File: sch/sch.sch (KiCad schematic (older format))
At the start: 6 parts, among them P1 Digital, P2 Analog, P3 CONN_1, P4 CONN_1, P5 CONN_1, P6 CONN_1

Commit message: Started schematic draft
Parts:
- added D? (x18): LED, symbol LED
- added D? (x6): D_Schottky, symbol D_Schottky
- added L? (x6): INDUCTOR, symbol INDUCTOR
- added R? (x26): R, symbol R
- added U? (x6): PT4115, symbol PT4115
- added U? (x2): LM741, symbol LM741
- added U?: 74LS595, symbol 74LS595
- added U?: 74LS165, symbol 74LS165
- added U?: 7805, symbol 7805
- added U? (x2): DS18B20, symbol DS18B20
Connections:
- net labels added: +BATT, -9VA, CLK, CLK2, DIM1, DIM2, DIM3, DIM4, DIM5, DIM6, L0, L1, L2, L3, L4, L5, L6, L7, LP0, LP1, LP2, LP3, LP4, LP5, LP6, LP7, PH, SALINITY, SER_IN, SER_OUT, T0, T1, ~LD
- wire segments 35 -> 181
- no-connect marks 4 -> 6

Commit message: More schematic work
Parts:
- removed U? (x2): LM741, symbol LM741
- added C? (x2): C, symbol C
- added C? (x2): CP, symbol CP
- added P? (x2): CONN_01X02, symbol CONN_01X02
- added P?: BNC, symbol BNC
- added R?: R, symbol R
- added U? (x4): LM324, symbol LM324
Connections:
- net labels removed: -9VA
- wire segments 181 -> 193
- no-connect marks 6 -> 7
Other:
- note added: "TODO:\nSlave board interface\nWhat to do with spare io\n"

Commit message: Finished drafting and started correcting DRC
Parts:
- removed P?: CONN_01X02, symbol CONN_01X02
- added BT1: Battery, symbol Battery
- added P10, P13: CONN_01X02, symbol CONN_01X02
- added P5, P9: CONN_01X08, symbol CONN_01X08
- added P6: CONN_02X05, symbol CONN_02X05
- added R21, R22, R26, R31, R32, R33: R, symbol R
- added U8, U9: DS18B20, symbol DS18B20
- R17, R19, R20, R29, R30, R6: renamed from R?; value R -> 0.13
- gave numbers to parts that had none: 69
- renumbered P3 to P1, P4 to P2, P5 to P3, P6 to P4, P1 to P7, P2 to P8
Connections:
- net labels added: AUG0, AUG1, AUX1, AUX2, PHG, SAG, TS0, TS1, VDD
- wire segments 193 -> 239
- no-connect marks 7 -> 12
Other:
- note added: "MOUNT ON MASTER"
- note added: "MOUNT ON SLAVE"
- note removed: "TODO:\nSlave board interface\nWhat to do with spare io\n"
- moved on the sheet: P11, P12, R23, R24, R25, R27, R28

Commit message: Schematic ready for layout, started layout work
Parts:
- removed P10, P12, P13: CONN_01X02, symbol CONN_01X02
- removed P5, P9: CONN_01X08, symbol CONN_01X08
- removed R1, R10, R11, R12, R13, R14, R15, R16, R18, R2, R3, R4, R5, R7, R8, R9: R, symbol R
- removed U1: 74LS595, symbol 74LS595
- removed U3: 74LS165, symbol 74LS165
- added C1: C, Capacitors_SMD:C_1206_HandSoldering, symbol C
- added P1: CONN_01X02, Connect:PINHEAD1-2, symbol CONN_01X02
- added P3, P4: CONN_01X06, Connect:PINHEAD1-6, symbol CONN_01X06
- added U8: SALINITY_AND_LEVEL_SENSOR, symbol SALINITY_AND_LEVEL_SENSOR
- BT1: footprint (none) -> Connect:bornier2
- C2: renamed from C1; footprint (none) -> Capacitors_ThroughHole:C_Radial_D5_L6_P2.5
- C3: renamed from C2; footprint (none) -> Capacitors_SMD:C_1206_HandSoldering
- C4: renamed from C3; footprint (none) -> Capacitors_SMD:C_1206_HandSoldering
- C5: renamed from C4; footprint (none) -> Capacitors_ThroughHole:C_Radial_D5_L6_P2.5
- D19: renamed from D16; footprint (none) -> Diodes_SMD:DO-214AB_Handsoldering
- D20: renamed from D24; footprint (none) -> Diodes_SMD:DO-214AB_Handsoldering
- D5: renamed from D4; footprint (none) -> Diodes_SMD:DO-214AB_Handsoldering
- D6: renamed from D8; footprint (none) -> Diodes_SMD:DO-214AB_Handsoldering
- D7: renamed from D15; footprint (none) -> Diodes_SMD:DO-214AB_Handsoldering
- D8: renamed from D23; footprint (none) -> Diodes_SMD:DO-214AB_Handsoldering
- L1, L2, L3, L6: footprint (none) -> Inductors_NEOSID:Neosid_Inductor_Ms95
- L4: renamed from L5; footprint (none) -> Inductors_NEOSID:Neosid_Inductor_Ms95
- L5: renamed from L4; footprint (none) -> Inductors_NEOSID:Neosid_Inductor_Ms95
- P2: renamed from P6; footprint (none) -> Connect:IDC_Header_Straight_10pins
- P5: renamed from P11; footprint (none) -> Connect:bnc-ci
- R1: renamed from R6; footprint (none) -> Resistors_SMD:R_1206_HandSoldering
- R10: renamed from R22; footprint (none) -> Resistors_SMD:R_0805_HandSoldering
- R11: renamed from R26; footprint (none) -> Resistors_SMD:R_0805_HandSoldering
- R12: renamed from R31; footprint (none) -> Resistors_SMD:R_0805_HandSoldering
- R13: renamed from R32; footprint (none) -> Resistors_SMD:R_0805_HandSoldering
- R14: renamed from R33; footprint (none) -> Resistors_SMD:R_0805_HandSoldering
- R15: renamed from R24; footprint (none) -> Resistors_SMD:R_0805_HandSoldering
- R16: renamed from R25; footprint (none) -> Resistors_SMD:R_0805_HandSoldering
- R17: renamed from R28; footprint (none) -> Resistors_SMD:R_0805_HandSoldering
- R2: renamed from R17; footprint (none) -> Resistors_SMD:R_1206_HandSoldering
- R3: renamed from R19; footprint (none) -> Resistors_SMD:R_1206_HandSoldering
- R4: renamed from R29; footprint (none) -> Resistors_SMD:R_1206_HandSoldering
- R5: renamed from R20; footprint (none) -> Resistors_SMD:R_1206_HandSoldering
- R6: renamed from R30; footprint (none) -> Resistors_SMD:R_1206_HandSoldering
- R7: renamed from R23; footprint (none) -> Resistors_SMD:R_0805_HandSoldering
- R8: renamed from R27; footprint (none) -> Resistors_SMD:R_0805_HandSoldering
- R9: renamed from R21; footprint (none) -> Resistors_SMD:R_0805_HandSoldering
- U1: renamed from U2; footprint (none) -> TO_SOT_Packages_SMD:SC-70-6_Handsoldering
- U10: renamed from U6; footprint (none) -> TO_SOT_Packages_THT:TO-92_Inline_Narrow_Oval
- U11: renamed from U7; footprint (none) -> TO_SOT_Packages_THT:TO-92_Inline_Narrow_Oval
- U12: renamed from U8; footprint (none) -> TO_SOT_Packages_THT:TO-92_Inline_Narrow_Oval
- U13: renamed from U9; footprint (none) -> TO_SOT_Packages_THT:TO-92_Inline_Narrow_Oval
- U2: renamed from U4; footprint (none) -> TO_SOT_Packages_SMD:SC-70-6_Handsoldering
- U3: renamed from U10; footprint (none) -> TO_SOT_Packages_SMD:SC-70-6_Handsoldering
- U4: renamed from U13; footprint (none) -> TO_SOT_Packages_SMD:SC-70-6_Handsoldering
- U5: renamed from U11; footprint (none) -> TO_SOT_Packages_SMD:SC-70-6_Handsoldering
- U6: renamed from U14; footprint (none) -> TO_SOT_Packages_SMD:SC-70-6_Handsoldering
- U7: renamed from U12; footprint (none) -> SMD_Packages:SOIC-14_N
- U9: renamed from U5; footprint (none) -> TO_SOT_Packages_THT:TO-220_Neutral123_Vertical_LargePads
- renumbered D6 to D10, D10 to D11, D18 to D12, D3 to D13, D7 to D14, D11 to D15, D19 to D16, D12 to D17, D20 to D18, D5 to D2, D13 to D21, D21 to D22, D14 to D23, D22 to D24, D9 to D3, D17 to D4, D2 to D9, P3 to P10, P4 to P11, P7 to P6, P8 to P7, P1 to P8, P2 to P9
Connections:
- net labels added: AUX, CAL0, CAL0_PROBE, CAL1, CAL1_PROBE, MEAS, MEAS_PROBE, O_CAL0, O_CAL0_PROBE, O_CAL1, O_CAL1_PROBE, O_MEAS, O_MEAS_PROBE
- net labels removed: +3.3V, AUG0, AUG1, AUX1, AUX2, CLK, CLK2, L0, L1, L2, L3, L4, L5, L6, L7, LP0, LP1, LP2, LP3, LP4, LP5, LP6, LP7, SAG, SALINITY, SER_IN, SER_OUT, VDD, ~LD
- wire segments 239 -> 213
- no-connect marks 12 -> 9
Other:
- moved on the sheet: P2, P5, R10, R11, R12, R13, R14, R7, R8, R9

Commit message: Started placement
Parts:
- removed D1, D10, D11, D12, D17, D18, D2, D22, D3, D4, D9: LED, symbol LED
- removed U9: 7805, TO_SOT_Packages_THT:TO-220_Neutral123_Vertical_LargePads, symbol 7805
- added U9: LM7805CT, Power_Integrations:TO-220, symbol LM7805CT
- D13, D14, D15, D16, D21, D23, D24: footprint (none) -> led:POWER_LED
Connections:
- wire segments 213 -> 208
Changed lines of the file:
@@
 Vin
-$Comp
-L LED D1
-U 1 1 5793CCBE
-P 1100 800
-F 0 "D1" H 1100 900 50  0000 C CNN
-F 1 "LED" H 1100 700 50  0000 C CNN
-F 2 "" H 1100 800 50  0001 C CNN
-F 3 "" H 1100 800 50  0000 C CNN
-	1    1100 800
-	1    0    0    -1
-$EndComp
 $Comp
 L INDUCTOR L1
@@
 $EndComp
 $Comp
-L LED D9
-U 1 1 5793E11C
-P 1550 800
-F 0 "D9" H 1550 900 50  0000 C CNN
-F 1 "LED" H 1550 700 50  0000 C CNN
-F 2 "" H 1550 800 50  0001 C CNN
-F 3 "" H 1550 800 50  0000 C CNN
-	1    1550 800
-	1    0    0    -1
-$EndComp
-$Comp
 L LED D13
 U 1 1 5793E17F
@@
 F 0 "D13" H 2000 900 50  0000 C CNN
 F 1 "LED" H 2000 700 50  0000 C CNN
-F 2 "" H 2000 800 50  0001 C CNN
+F 2 "led:POWER_LED" H 2000 800 50  0001 C CNN
 F 3 "" H 2000 800 50  0000 C CNN
 	1    2000 800
@@
 F 3 "" H 800 1850 50  0000 C CNN
 	1    800  1850
-	1    0    0    -1
-$EndComp
-$Comp
-L LED D2
-U 1 1 5793EAC5
-P 1100 2400
-F 0 "D2" H 1100 2500 50  0000 C CNN
-F 1 "LED" H 1100 2300 50  0000 C CNN
-F 2 "" H 1100 2400 50  0001 C CNN
-F 3 "" H 1100 2400 50  0000 C CNN
-	1    1100 2400
 	1    0    0    -1
 $EndComp
@@
 $EndComp
 $Comp
-L LED D10
-U 1 1 5793EAF1
-P 1550 2400
-F 0 "D10" H 1550 2500 50  0000 C CNN
-F 1 "LED" H 1550 2300 50  0000 C CNN
-F 2 "" H 1550 2400 50  0001 C CNN
-F 3 "" H 1550 2400 50  0000 C CNN
-	1    1550 2400
-	1    0    0    -1
-$EndComp
-$Comp
 L LED D14
 U 1 1 5793EAF7
@@
 F 0 "D14" H 2000 2500 50  0000 C CNN
 F 1 "LED" H 2000 2300 50  0000 C CNN
-F 2 "" H 2000 2400 50  0001 C CNN
+F 2 "led:POWER_LED" H 2000 2400 50  0001 C CNN
 F 3 "" H 2000 2400 50  0000 C CNN
 	1    2000 2400
@@
 F 3 "" H 800 3450 50  0000 C CNN
 	1    800  3450
-	1    0    0    -1
-$EndComp
-$Comp
-L LED D3
-U 1 1 5793EE50
-P 1100 3950
-F 0 "D3" H 1100 4050 50  0000 C CNN
-F 1 "LED" H 1100 3850 50  0000 C CNN
-F 2 "" H 1100 3950 50  0001 C CNN
-F 3 "" H 1100 3950 50  0000 C CNN
-	1    1100 3950
 	1    0    0    -1
 $EndComp
@@
 $EndComp
 $Comp
-L LED D11
-U 1 1 5793EE7C
-P 1550 3950
-F 0 "D11" H 1550 4050 50  0000 C CNN
-F 1 "LED" H 1550 3850 50  0000 C CNN
-F 2 "" H 1550 3950 50  0001 C CNN
-F 3 "" H 1550 3950 50  0000 C CNN
-	1    1550 3950
-	1    0    0    -1
-$EndComp
-$Comp
 L LED D15
 U 1 1 5793EE82
@@
 F 0 "D15" H 2000 4050 50  0000 C CNN
 F 1 "LED" H 2000 3850 50  0000 C CNN
-F 2 "" H 2000 3950 50  0001 C CNN
+F 2 "led:POWER_LED" H 2000 3950 50  0001 C CNN
 F 3 "" H 2000 3950 50  0000 C CNN
 	1    2000 3950
@@
 F 3 "" H 800 5000 50  0000 C CNN
 	1    800  5000
-	1    0    0    -1
-$EndComp
-$Comp
-L LED D4
-U 1 1 5793EE9A
-P 1100 5550
-F 0 "D4" H 1100 5650 50  0000 C CNN
-F 1 "LED" H 1100 5450 50  0000 C CNN
-F 2 "" H 1100 5550 50  0001 C CNN
-F 3 "" H 1100 5550 50  0000 C CNN
-	1    1100 5550
 	1    0    0    -1
 $EndComp
@@
 $EndComp
 $Comp
-L LED D12
-U 1 1 5793EEC6
-P 1550 5550
-F 0 "D12" H 1550 5650 50  0000 C CNN
-F 1 "LED" H 1550 5450 50  0000 C CNN
-F 2 "" H 1550 5550 50  0001 C CNN
-F 3 "" H 1550 5550 50  0000 C CNN
-	1    1550 5550
-	1    0    0    -1
-$EndComp
-$Comp
 L LED D16
 U 1 1 5793EECC
@@
 F 0 "D16" H 2000 5650 50  0000 C CNN
 F 1 "LED" H 2000 5450 50  0000 C CNN
-F 2 "" H 2000 5550 50  0001 C CNN
+F 2 "led:POWER_LED" H 2000 5550 50  0001 C CNN
 F 3 "" H 2000 5550 50  0000 C CNN
 	1    2000 5550
@@
 F 3 "" H 800 6600 50  0000 C CNN
 	1    800  6600
-	1    0    0    -1
-$EndComp
-$Comp
-L LED D17
-U 1 1 5793F14C
-P 2850 3950
-F 0 "D17" H 2850 4050 50  0000 C CNN
-F 1 "LED" H 2850 3850 50  0000 C CNN
-F 2 "" H 2850 3950 50  0001 C CNN
-F 3 "" H 2850 3950 50  0000 C CNN
-	1    2850 3950
 	1    0    0    -1
 $EndComp
@@
 F 0 "D21" H 3300 4050 50  0000 C CNN
 F 1 "LED" H 3300 3850 50  0000 C CNN
-F 2 "" H 3300 3950 50  0001 C CNN
+F 2 "led:POWER_LED" H 3300 3950 50  0001 C CNN
 F 3 "" H 3300 3950 50  0000 C CNN
 	1    3300 3950
@@
 F 0 "D23" H 3750 4050 50  0000 C CNN
 F 1 "LED" H 3750 3850 50  0000 C CNN
-F 2 "" H 3750 3950 50  0001 C CNN
+F 2 "led:POWER_LED" H 3750 3950 50  0001 C CNN
 F 3 "" H 3750 3950 50  0000 C CNN
 	1    3750 3950
@@
 F 3 "" H 2550 5000 50  0000 C CNN
 	1    2550 5000
-	1    0    0    -1
-$EndComp
-$Comp
-L LED D18
-U 1 1 5793F196
-P 2850 5550
-F 0 "D18" H 2850 5650 50  0000 C CNN
-F 1 "LED" H 2850 5450 50  0000 C CNN
-F 2 "" H 2850 5550 50  0001 C CNN
-F 3 "" H 2850 5550 50  0000 C CNN
-	1    2850 5550
 	1    0    0    -1
 $EndComp
@@
 $EndComp
 $Comp
-L LED D22
-U 1 1 5793F1C2
-P 3300 5550
-F 0 "D22" H 3300 5650 50  0000 C CNN
-F 1 "LED" H 3300 5450 50  0000 C CNN
-F 2 "" H 3300 5550 50  0001 C CNN
-F 3 "" H 3300 5550 50  0000 C CNN
-	1    3300 5550
-	1    0    0    -1
-$EndComp
-$Comp
 L LED D24
 U 1 1 5793F1C8
@@
 F 0 "D24" H 3750 5650 50  0000 C CNN
 F 1 "LED" H 3750 5450 50  0000 C CNN
-F 2 "" H 3750 5550 50  0001 C CNN
+F 2 "led:POWER_LED" H 3750 5550 50  0001 C CNN
 F 3 "" H 3750 5550 50  0000 C CNN
 	1    3750 5550
@@
 F 3 "" H 5700 7100 50  0000 C CNN
 	1    5700 7100
-	1    0    0    -1
-$EndComp
-$Comp
-L 7805 U9
-U 1 1 57940F94
-P 7550 4100
-F 0 "U9" H 7700 3904 50  0000 C CNN
-F 1 "7805" H 7550 4300 50  0000 C CNN
-F 2 "TO_SOT_Packages_THT:TO-220_Neutral123_Vertical_LargePads" H 7550 4100 50  0001 C CNN
-F 3 "" H 7550 4100 50  0000 C CNN
-	1    7550 4100
 	1    0    0    -1
 $EndComp
@@
 	900  800  900  850
 Wire Wire Line
-	1300 800  1350 800
-Wire Wire Line
-	1750 800  1800 800
+	900  800  1800 800
 Wire Wire Line
 	1700 1850 1750 1850
@@
 	900  2400 900  2450
 Wire Wire Line
-	1300 2400 1350 2400
-Wire Wire Line
-	1750 2400 1800 2400
+	900  2400 1800 2400
 Wire Wire Line
 	1700 3450 1750 3450
@@
 	900  3950 900  4000
 Wire Wire Line
-	1300 3950 1350 3950
-Wire Wire Line
-	1750 3950 1800 3950
+	900  3950 1800 3950
 Wire Wire Line
 	1700 5000 1750 5000
@@
 	900  5550 900  5600
 Wire Wire Line
-	1300 5550 1350 5550
-Wire Wire Line
-	1750 5550 1800 5550
+	900  5550 1800 5550
 Wire Wire Line
 	1700 6600 1750 6600
@@
 	2650 3950 2650 4000
 Wire Wire Line
-	3050 3950 3100 3950
+	2650 3950 3100 3950
 Wire Wire Line
 	3500 3950 3550 3950
@@
 	2650 5550 2650 5600
 Wire Wire Line
-	3050 5550 3100 5550
-Wire Wire Line
-	3500 5550 3550 5550
+	2650 5550 3550 5550
 Wire Wire Line
 	3450 6600 3500 6600
@@
 Text Label 8150 1900 0    60   ~ 0
 TS1
+$Comp
+L LM7805CT U9
+U 1 1 5796A95B
+P 7550 4100
+F 0 "U9" H 7350 4300 50  0000 C CNN
+F 1 "LM7805CT" H 7550 4300 50  0000 L CNN
+F 2 "Power_Integrations:TO-220" H 7550 4200 50  0000 C CIN
+F 3 "" H 7550 4100 50  0000 C CNN
+	1    7550 4100
+	1    0    0    -1
+$EndComp
 $EndSCHEMATC

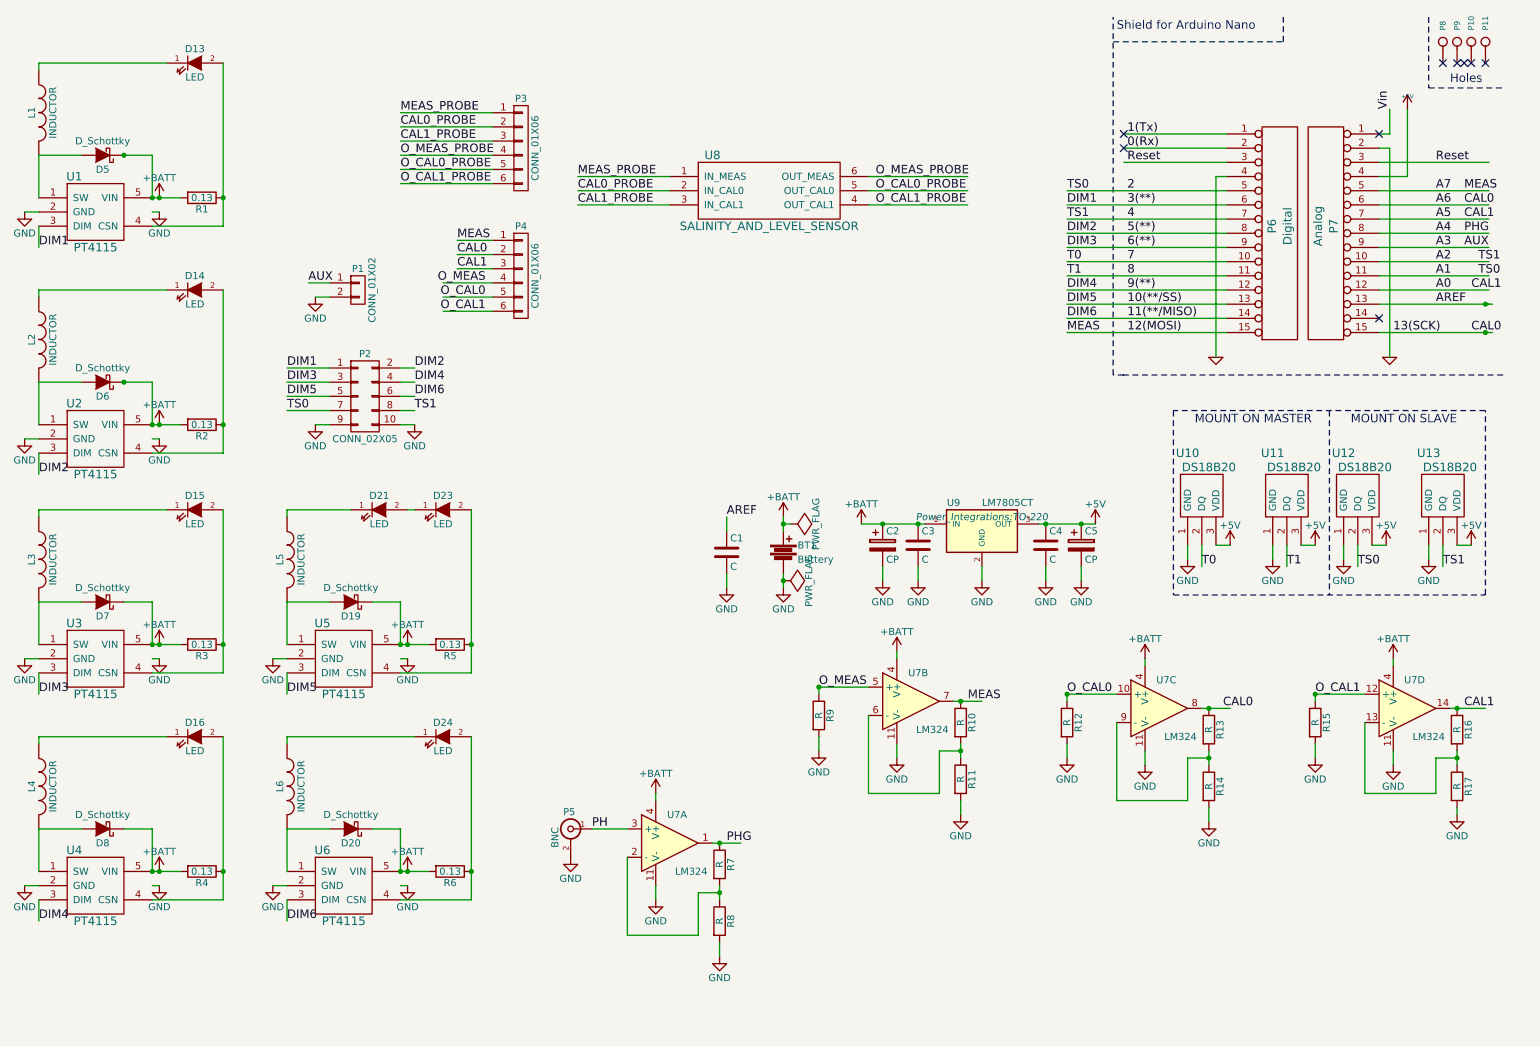
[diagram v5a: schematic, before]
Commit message: Added some footprint libraries and started layout
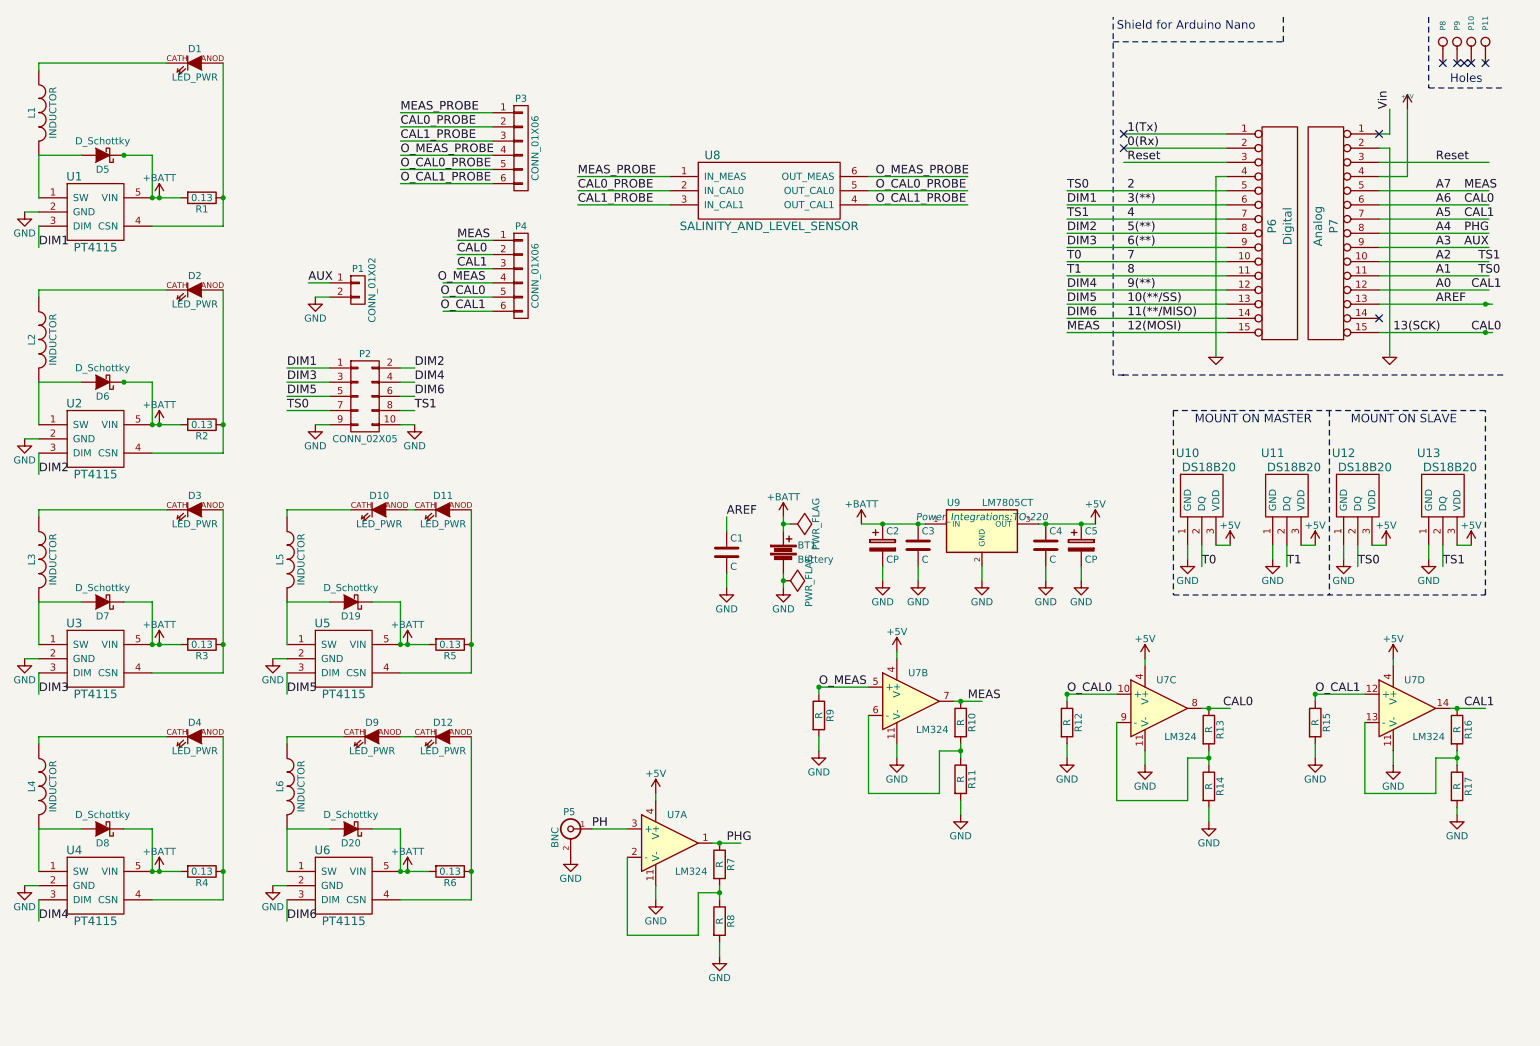
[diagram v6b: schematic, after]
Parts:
- removed D13, D14, D15, D16, D21, D23, D24: LED, led:POWER_LED, symbol LED
- added D1, D10, D11, D12, D2, D3, D4, D9: LED_PWR, sch:lumiled-2-LAMBERTIAN, symbol LED_PWR
- U1, U2, U3, U4, U5, U6: footprint TO_SOT_Packages_SMD:SC-70-6_Handsoldering -> TO_SOT_Packages_SMD:SOT89-5_Housing_Handsoldering
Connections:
- wire segments 208 -> 203
